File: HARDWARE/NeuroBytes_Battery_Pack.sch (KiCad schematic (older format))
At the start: 12 parts, among them P1 JST_GH_5-pos, SW1 Switch_DPDT, U1 LDL212_LDO

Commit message: updated to include two 5-pin JST connectors and side-mtg switch. Moved LED to center.
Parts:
- removed SW1: Switch_DPDT, KiCad_Footprints:ZF_SW_Slide_DPDT_SMD, symbol Switch_DPDT
- added P2: JST_GH_5-pos, KiCad_Footprints:ZF_CONN_JST_GH_5POS, symbol CONN_01X05
- added R1, R3, R7: R_Small, KiCad_Footprints:ZF_SMD_NonPol_0402, symbol R_Small
- added SW1: Switch_SPDT, KiCad_Footprints:ZF_SW_PCM12SMTR, symbol Switch_SPDT
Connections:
- net GND: now also P2.1 (P1), R1.2, R3.2, SW1.3
- net at C1.1, F1.1, U1.4 (VIN): now also SW1.1
- net at C2.1, D1.2 (A), P1.5 (P5)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: now also P2.5 (P5), R7.2
- net at U1.6 (EN): now also SW1.2
- new net: P2.4 (P4), R1.1
- new net: P2.3 (P3), R3.1
- new net: P2.2 (P2), R7.1
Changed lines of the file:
@@
 LIBS:valves
 LIBS:NeuroTinker_schematic_symbols
-LIBS:NeuroBytes_Battery_Power_4xAA-cache
+LIBS:NeuroBytes_Battery_Pack-cache
 EELAYER 25 0
 EELAYER END
@@
 Wire Wire Line
 	7100 1850 8000 1850
-$Comp
-L Switch_DPDT SW1
-U 1 1 5925F129
-P 3700 1750
-F 0 "SW1" H 3700 1350 60  0000 C CNN
-F 1 "Switch_DPDT" H 3700 2025 60  0000 C CNN
-F 2 "KiCad_Footprints:ZF_SW_Slide_DPDT_SMD" H 3700 1750 60  0001 C CNN
-F 3 "" H 3700 1750 60  0001 C CNN
-F 4 "No" H 3700 1750 60  0001 C CNN "Subs Allowed"
-F 5 "Yes" H 3700 1750 60  0001 C CNN "RoHS"
-	1    3700 1750
-	1    0    0    1
-$EndComp
 Wire Wire Line
 	5650 1250 8000 1250
@@
 	6200 2500 6200 1900
 Wire Wire Line
-	7350 1250 7350 1750
+	7350 1250 7350 3150
 Connection ~ 7350 1250
 Connection ~ 7500 1850
@@
 	7500 1550 7500 1850
 Wire Wire Line
-	8000 1250 8000 1450
+	8000 1250 8000 2850
+Wire Wire Line
+	7100 3250 8000 3250
+Connection ~ 7500 3250
+Wire Wire Line
+	7650 2950 7500 2950
+Wire Wire Line
+	7650 3050 7500 3050
+Connection ~ 7500 3050
+Wire Wire Line
+	8000 3150 7850 3150
+Wire Wire Line
+	7350 3150 7650 3150
+Wire Wire Line
+	8000 2950 7850 2950
+Wire Wire Line
+	7850 3050 8000 3050
+$Comp
+L R_Small R1
+U 1 1 59C16211
+P 7750 2950
+F 0 "R1" V 7700 2750 50  0000 L CNN
+F 1 "R_Small" V 7250 2850 50  0000 L CNN
+F 2 "KiCad_Footprints:ZF_SMD_NonPol_0402" H 7750 2950 50  0001 C CNN
+F 3 "" H 7750 2950 50  0000 C CNN
+F 4 "No" H 7750 2950 60  0001 C CNN "Subs Allowed"
+F 5 "Yes" H 7750 2950 60  0001 C CNN "RoHS"
+	1    7750 2950
+	0    1    1    0
+$EndComp
+$Comp
+L R_Small R3
+U 1 1 59C16219
+P 7750 3050
+F 0 "R3" V 7700 2850 50  0000 L CNN
+F 1 "R_Small" V 7250 2950 50  0000 L CNN
+F 2 "KiCad_Footprints:ZF_SMD_NonPol_0402" H 7750 3050 50  0001 C CNN
+F 3 "" H 7750 3050 50  0000 C CNN
+F 4 "No" H 7750 3050 60  0001 C CNN "Subs Allowed"
+F 5 "Yes" H 7750 3050 60  0001 C CNN "RoHS"
+	1    7750 3050
+	0    1    1    0
+$EndComp
+$Comp
+L R_Small R7
+U 1 1 59C16221
+P 7750 3150
+F 0 "R7" V 7700 2950 50  0000 L CNN
+F 1 "R_Small" V 7250 3050 50  0000 L CNN
+F 2 "KiCad_Footprints:ZF_SMD_NonPol_0402" H 7750 3150 50  0001 C CNN
+F 3 "" H 7750 3150 50  0000 C CNN
+F 4 "No" H 7750 3150 60  0001 C CNN "Subs Allowed"
+F 5 "Yes" H 7750 3150 60  0001 C CNN "RoHS"
+	1    7750 3150
+	0    1    1    0
+$EndComp
+$Comp
+L CONN_01X05 P2
+U 1 1 59C16229
+P 8200 3050
+F 0 "P2" H 8200 3350 50  0000 C CNN
+F 1 "JST_GH_5-pos" V 8300 3050 50  0000 C CNN
+F 2 "KiCad_Footprints:ZF_CONN_JST_GH_5POS" H 8400 3450 50  0000 C CNN
+F 3 "" H 8200 3050 50  0000 C CNN
+F 4 "No" H 8200 3050 60  0001 C CNN "Subs Allowed"
+F 5 "Yes" H 8200 3050 60  0001 C CNN "RoHS"
+	1    8200 3050
+	1    0    0    1
+$EndComp
+Wire Wire Line
+	7500 2950 7500 3250
+Connection ~ 8000 1450
+Connection ~ 7350 1750
+$Comp
+L GND #PWR06
+U 1 1 59C1639A
+P 7100 3600
+F 0 "#PWR06" H 7100 3350 50  0001 C CNN
+F 1 "GND" H 7100 3450 50  0000 C CNN
+F 2 "" H 7100 3600 50  0001 C CNN
+F 3 "" H 7100 3600 50  0001 C CNN
+	1    7100 3600
+	1    0    0    -1
+$EndComp
+Wire Wire Line
+	7100 3600 7100 3250
+$Comp
+L Switch_SPDT SW1
+U 1 1 59C16AD6
+P 3700 1750
+F 0 "SW1" H 3700 1350 60  0000 C CNN
+F 1 "Switch_SPDT" H 3700 2025 60  0000 C CNN
+F 2 "KiCad_Footprints:ZF_SW_PCM12SMTR" H 3700 1750 60  0001 C CNN
+F 3 "" H 3700 1750 60  0001 C CNN
+F 4 "No" H 3700 1750 60  0001 C CNN "Subs Allowed"
+F 5 "Yes" H 3700 1750 60  0001 C CNN "RoHS"
+	1    3700 1750
+	-1   0    0    -1
+$EndComp
 $EndSCHEMATC

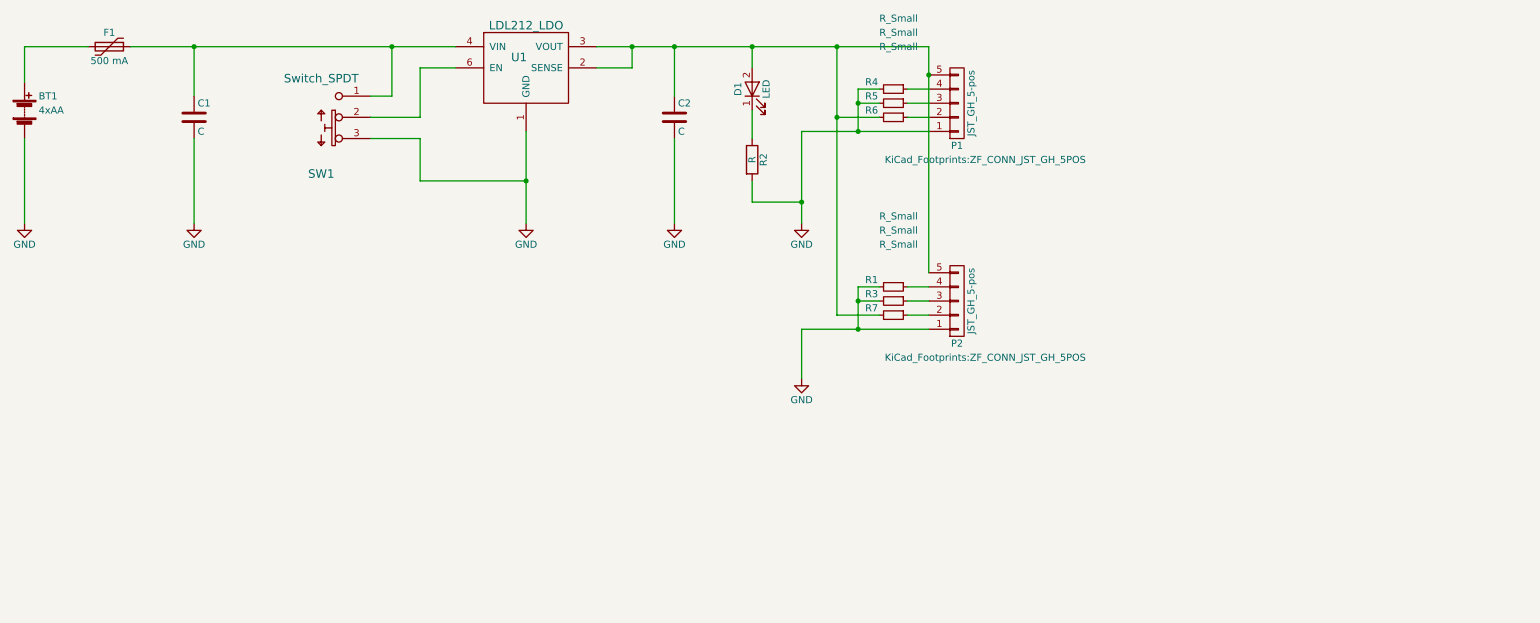
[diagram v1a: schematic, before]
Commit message: updated component labels and regenerated netlist. generated BOM. minor page layout updates.
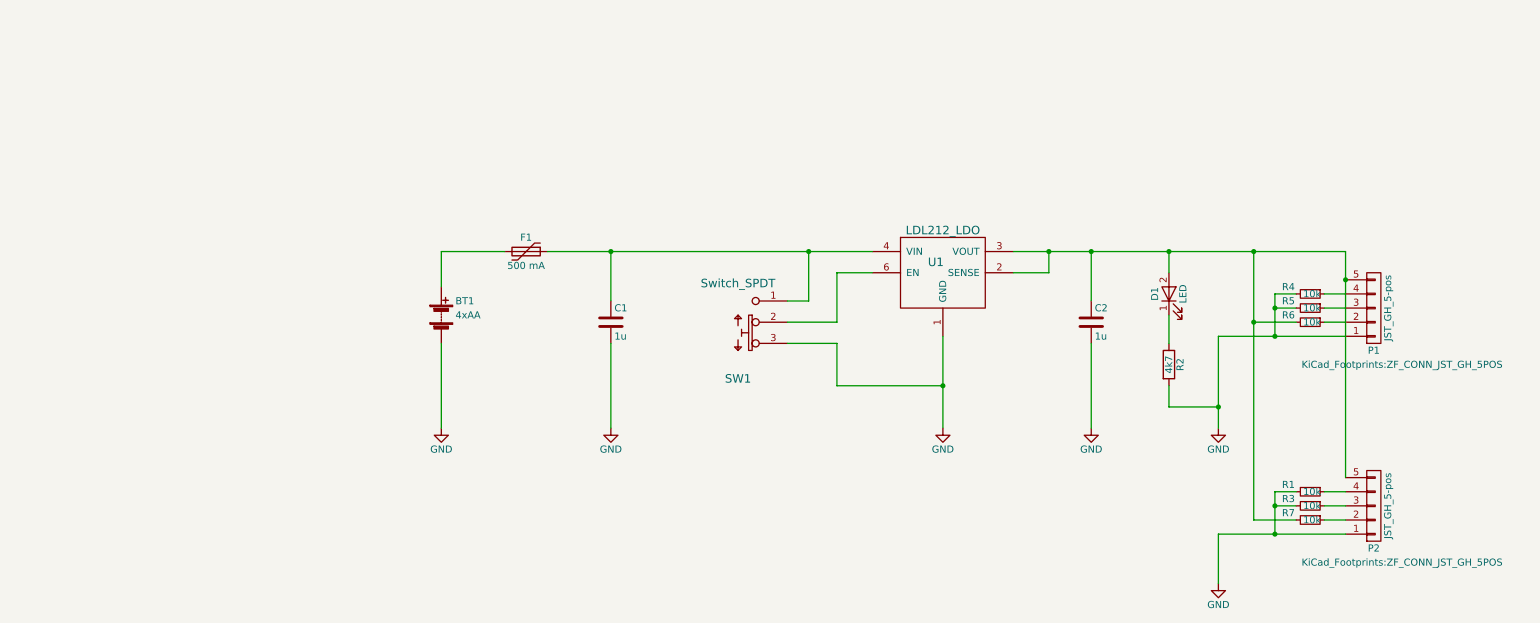
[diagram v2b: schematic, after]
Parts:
- BT1: Link (none) -> https://www.digikey.com/product-detail/en/mpd-memory-protec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; Mfr (none) -> MPD (Memory Protection Devices); Mfr Part # (none) -> BC4AAPC; Package (none) -> THT
- C1, C2: value C -> 1u; Link (none) -> https://www.digikey.com/product-detail/en/taiyo-yuden/LMK10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; Mfr (none) -> Taiyo Yuden; Mfr Part # (none) -> LMK107B7105KA-T; Package (none) -> C0603; Subs Allowed No -> Yes
- D1: Link (none) -> https://www.digikey.com/product-detail/en/rohm-semiconducto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; Mfr (none) -> Rohm Semiconductor; Mfr Part # (none) -> SMLP13EC8TT86; Package (none) -> L0402
- F1: Link (none) -> https://www.digikey.com/product-detail/en/bel-fuse-inc/0ZCH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; Mfr (none) -> Bel Fuse Inc.; Mfr Part # (none) -> 0ZCH0050FF2G; Package (none) -> F1210; Subs Allowed No -> Yes
- P1, P2: Link (none) -> https://www.digikey.com/product-detail/en/jst-sales-america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; Mfr (none) -> JST; Mfr Part # (none) -> SM05B-GHS-TB(LF)(SN); Package (none) -> SMT
- R1, R3, R4, R5, R6, R7: value R_Small -> 10k; Link (none) -> https://www.digikey.com/product-detail/en/yageo/RC0402FR-07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; Mfr (none) -> Yageo; Mfr Part # (none) -> RC0402FR-0710KL; Package (none) -> R0402; Subs Allowed No -> Yes
- R2: value R -> 4k7; Link (none) -> https://www.digikey.com/product-detail/en/yageo/RC0402FR-07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; Mfr (none) -> Yageo; Mfr Part # (none) -> RC0402FR-074K7L; Package (none) -> R0402; Subs Allowed No -> Yes
- SW1: Link (none) -> https://www.digikey.com/product-detail/en/c-k/PCM12SMTR/401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; Mfr (none) -> C&K; Mfr Part # (none) -> PCM12SMTR; Package (none) -> SMT
- U1: Link (none) -> https://www.digikey.com/product-detail/en/stmicroelectronic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; Mfr (none) -> ST Microelectronics; Mfr Part # (none) -> LDL212PU50R; Package (none) -> 6DFN
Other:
- moved on the sheet: BT1, C1, D1, F1, P1, R2, R4, SW1, U1
